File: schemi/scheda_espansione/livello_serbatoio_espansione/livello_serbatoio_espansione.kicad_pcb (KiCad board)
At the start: 2 copper layers, 70 x 50 mm, 264 parts, among them J1 exp1, J2 exp_spi, J3 exp2

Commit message: modifiche scheda definitiva (rev. C)
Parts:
- removed the REF** at (123.0, 62.9)
- removed the REF** at (156.0, 91.0)
- removed the REF** at (112.9, 78.2)
- removed the REF** at (171.3, 58.8)
- removed the REF** at (168.8, 58.8)
- removed the REF** at (166.2, 58.8)
- removed the REF** at (163.7, 58.8)
- removed the REF** at (161.2, 58.8)
- removed the REF** at (173.9, 58.8)
- removed the REF** at (173.8, 80.9)
- removed the REF** at (171.3, 80.9)
- removed the REF** at (168.8, 80.9)
- removed the REF** at (163.7, 91.0)
- removed the REF** at (166.2, 80.9)
- removed the REF** at (163.7, 80.9)
- removed the REF** at (161.1, 78.3)
- removed the REF** at (158.6, 78.3)
- removed the REF** at (156.1, 78.3)
- removed the REF** at (153.5, 78.3)
- removed the REF** at (118.0, 75.7)
- removed the REF** at (115.5, 75.7)
- removed the REF** at (112.9, 75.7)
- removed the REF** at (171.3, 56.3)
- removed the REF** at (171.3, 91.0)
- removed the REF** at (168.8, 56.3)
- removed the REF** at (166.2, 56.3)
- removed the REF** at (163.7, 56.3)
- removed the REF** at (161.2, 56.3)
- removed the REF** at (173.9, 56.3)
- removed the REF** at (173.8, 78.3)
- removed the REF** at (171.3, 78.3)
- removed the REF** at (168.8, 78.3)
- removed the REF** at (166.2, 78.3)
- removed the REF** at (163.7, 78.3)
- removed the REF** at (166.2, 91.0)
- removed the REF** at (161.1, 75.8)
- removed the REF** at (158.6, 75.8)
- removed the REF** at (156.1, 75.8)
- removed the REF** at (153.5, 75.8)
- removed the REF** at (118.0, 73.2)
- removed the REF** at (115.5, 73.2)
- removed the REF** at (112.9, 73.2)
- removed the REF** at (171.3, 53.8)
- removed the REF** at (168.8, 53.8)
- removed the REF** at (166.2, 53.8)
- removed the REF** at (153.5, 91.0)
- removed the REF** at (163.7, 53.8)
- removed the REF** at (161.2, 53.8)
- removed the REF** at (173.9, 53.8)
- removed the REF** at (173.8, 75.8)
- removed the REF** at (171.3, 75.8)
- removed the REF** at (168.8, 75.8)
- removed the REF** at (166.2, 75.8)
- removed the REF** at (163.7, 75.8)
- removed the REF** at (161.1, 73.3)
- removed the REF** at (158.6, 73.3)
- removed the REF** at (158.6, 91.0)
- removed the REF** at (156.1, 73.3)
- removed the REF** at (153.5, 73.3)
- removed the REF** at (118.0, 70.6)
- removed the REF** at (115.5, 70.6)
- removed the REF** at (112.9, 70.6)
- removed the REF** at (171.3, 51.2)
- removed the REF** at (168.8, 51.2)
- removed the REF** at (166.2, 51.2)
- removed the REF** at (163.7, 51.2)
- removed the REF** at (161.2, 51.2)
- removed the REF** at (161.1, 91.0)
- removed the REF** at (173.9, 51.2)
- removed the REF** at (173.8, 73.3)
- removed the REF** at (171.3, 73.3)
- removed the REF** at (168.8, 73.3)
- removed the REF** at (166.2, 73.3)
- removed the REF** at (163.7, 73.3)
- removed the REF** at (173.9, 68.0)
- removed the REF** at (171.3, 68.0)
- removed the REF** at (168.8, 68.0)
- removed the REF** at (166.2, 68.0)
- removed the REF** at (168.8, 91.0)
- removed the REF** at (163.7, 68.0)
- removed the REF** at (161.2, 68.0)
- removed the REF** at (158.6, 68.0)
- removed the REF** at (156.1, 68.0)
- removed the REF** at (153.5, 68.0)
- removed the REF** at (151.0, 68.0)
- removed the REF** at (148.5, 68.0)
- removed the REF** at (145.9, 68.0)
- removed the REF** at (143.4, 68.0)
- removed the REF** at (140.8, 68.0)
- removed the REF** at (173.8, 91.0)
- removed the REF** at (138.3, 68.0)
- removed the REF** at (135.8, 68.0)
- removed the REF** at (133.2, 68.0)
- removed the REF** at (130.7, 68.0)
- removed the REF** at (128.1, 68.0)
- removed the REF** at (125.6, 68.0)
- removed the REF** at (118.0, 68.1)
- removed the REF** at (115.5, 68.1)
- removed the REF** at (112.9, 68.1)
- removed the REF** at (173.9, 65.4)
- removed the REF** at (161.1, 88.5)
- removed the REF** at (171.3, 65.4)
- removed the REF** at (168.8, 65.4)
- removed the REF** at (166.2, 65.4)
- removed the REF** at (163.7, 65.4)
- removed the REF** at (161.2, 65.4)
- removed the REF** at (158.6, 65.4)
- removed the REF** at (156.1, 65.4)
- removed the REF** at (153.5, 65.4)
- removed the REF** at (151.0, 65.4)
- removed the REF** at (148.5, 65.4)
- removed the REF** at (123.0, 65.4)
- removed the REF** at (158.6, 88.5)
- removed the REF** at (145.9, 65.4)
- removed the REF** at (143.4, 65.4)
- removed the REF** at (140.8, 65.4)
- removed the REF** at (138.3, 65.4)
- removed the REF** at (135.8, 65.4)
- removed the REF** at (133.2, 65.4)
- removed the REF** at (130.7, 65.4)
- removed the REF** at (128.1, 65.4)
- removed the REF** at (125.6, 65.4)
- removed the REF** at (118.0, 65.5)
- removed the REF** at (156.1, 88.5)
- removed the REF** at (115.5, 65.5)
- removed the REF** at (112.9, 65.5)
- removed the REF** at (173.9, 62.9)
- removed the REF** at (171.3, 62.9)
- removed the REF** at (168.8, 62.9)
- removed the REF** at (166.2, 62.9)
- removed the REF** at (163.7, 62.9)
- removed the REF** at (161.2, 62.9)
- removed the REF** at (158.6, 62.9)
- removed the REF** at (156.1, 62.9)
- removed the REF** at (153.5, 88.5)
- removed the REF** at (153.5, 62.9)
- removed the REF** at (151.0, 62.9)
- removed the REF** at (148.5, 62.9)
- removed the REF** at (145.9, 62.9)
- removed the REF** at (143.4, 62.9)
- removed the REF** at (140.8, 62.9)
- removed the REF** at (138.3, 62.9)
- removed the REF** at (135.8, 62.9)
- removed the REF** at (133.2, 62.9)
- removed the REF** at (130.7, 62.9)
- removed the REF** at (151.0, 91.0)
- removed the REF** at (128.1, 62.9)
- removed the REF** at (125.6, 62.9)
- removed the REF** at (118.0, 63.0)
- removed the REF** at (115.5, 63.0)
- removed the REF** at (112.9, 63.0)
- removed the REF** at (148.4, 91.0)
- removed the REF** at (145.9, 91.0)
- removed the REF** at (143.3, 91.0)
- removed the REF** at (140.8, 91.0)
- removed the REF** at (138.3, 91.0)
- removed the REF** at (135.7, 91.0)
- removed the REF** at (123.0, 68.0)
- removed the REF** at (133.2, 91.0)
- removed the REF** at (130.6, 91.0)
- removed the REF** at (128.1, 91.0)
- removed the REF** at (125.6, 91.0)
- removed the REF** at (123.0, 91.0)
- removed the REF** at (120.5, 91.0)
- removed the REF** at (117.9, 91.0)
- removed the REF** at (115.4, 91.0)
- removed the REF** at (112.9, 91.0)
- removed the REF** at (173.8, 88.5)
- removed the REF** at (115.4, 83.3)
- removed the REF** at (171.3, 88.5)
- removed the REF** at (168.8, 88.5)
- removed the REF** at (166.2, 88.5)
- removed the REF** at (163.7, 88.5)
- removed the REF** at (161.1, 86.0)
- removed the REF** at (158.6, 86.0)
- removed the REF** at (156.1, 86.0)
- removed the REF** at (153.5, 86.0)
- removed the REF** at (151.0, 88.5)
- removed the REF** at (148.4, 88.5)
- removed the REF** at (112.9, 80.8)
- removed the REF** at (145.9, 88.5)
- removed the REF** at (143.3, 88.5)
- removed the REF** at (140.8, 88.5)
- removed the REF** at (138.3, 88.5)
- removed the REF** at (135.7, 88.5)
- removed the REF** at (133.2, 88.5)
- removed the REF** at (130.6, 88.5)
- removed the REF** at (128.1, 88.5)
- removed the REF** at (125.6, 88.5)
- removed the REF** at (123.0, 88.5)
- removed the REF** at (118.0, 80.8)
- removed the REF** at (120.5, 88.5)
- removed the REF** at (117.9, 88.5)
- removed the REF** at (115.4, 88.5)
- removed the REF** at (112.9, 88.5)
- removed the REF** at (173.8, 86.0)
- removed the REF** at (171.3, 86.0)
- removed the REF** at (168.8, 86.0)
- removed the REF** at (166.2, 86.0)
- removed the REF** at (163.7, 86.0)
- removed the REF** at (161.1, 83.4)
- removed the REF** at (115.4, 80.8)
- removed the REF** at (158.6, 83.4)
- removed the REF** at (156.1, 83.4)
- removed the REF** at (153.5, 83.4)
- removed the REF** at (151.0, 85.9)
- removed the REF** at (148.4, 85.9)
- removed the REF** at (145.9, 85.9)
- removed the REF** at (143.3, 85.9)
- removed the REF** at (140.8, 85.9)
- removed the REF** at (138.3, 85.9)
- removed the REF** at (135.7, 85.9)
- removed the REF** at (112.9, 83.3)
- removed the REF** at (133.2, 85.9)
- removed the REF** at (130.6, 85.9)
- removed the REF** at (128.1, 85.9)
- removed the REF** at (125.6, 85.9)
- removed the REF** at (123.0, 85.9)
- removed the REF** at (120.5, 85.9)
- removed the REF** at (117.9, 85.9)
- removed the REF** at (115.4, 85.9)
- removed the REF** at (112.9, 85.9)
- removed the REF** at (173.8, 83.4)
- removed the REF** at (118.0, 83.3)
- removed the REF** at (171.3, 83.4)
- removed the REF** at (168.8, 83.4)
- removed the REF** at (166.2, 83.4)
- removed the REF** at (163.7, 83.4)
- removed the REF** at (161.1, 80.9)
- removed the REF** at (158.6, 80.9)
- removed the REF** at (156.1, 80.9)
- removed the REF** at (153.5, 80.9)
- removed the REF** at (118.0, 78.2)
- removed the REF** at (115.5, 78.2)
- removed TP1, TP12, TP23, TP27, TP5: GND, TestPoint:TestPoint_THTPad_D1.5mm_Drill0.7mm
- removed TP10: SPI_SCK, TestPoint:TestPoint_THTPad_D1.5mm_Drill0.7mm
- removed TP11: SPI_MISO, TestPoint:TestPoint_THTPad_D1.5mm_Drill0.7mm
- removed TP13: D9, TestPoint:TestPoint_THTPad_D1.5mm_Drill0.7mm
- removed TP14: D8, TestPoint:TestPoint_THTPad_D1.5mm_Drill0.7mm
- removed TP15: D7, TestPoint:TestPoint_THTPad_D1.5mm_Drill0.7mm
- removed TP16: D6, TestPoint:TestPoint_THTPad_D1.5mm_Drill0.7mm
- removed TP17: D5, TestPoint:TestPoint_THTPad_D1.5mm_Drill0.7mm
- removed TP18: A0, TestPoint:TestPoint_THTPad_D1.5mm_Drill0.7mm
- removed TP19: A1, TestPoint:TestPoint_THTPad_D1.5mm_Drill0.7mm
- removed TP2: SPI_MOSI, TestPoint:TestPoint_THTPad_D1.5mm_Drill0.7mm
- removed TP20: A2, TestPoint:TestPoint_THTPad_D1.5mm_Drill0.7mm
- removed TP21: A3, TestPoint:TestPoint_THTPad_D1.5mm_Drill0.7mm
- removed TP22: D4, TestPoint:TestPoint_THTPad_D1.5mm_Drill0.7mm
- removed TP24: D3, TestPoint:TestPoint_THTPad_D1.5mm_Drill0.7mm
- removed TP25: RV, TestPoint:TestPoint_THTPad_D1.5mm_Drill0.7mm
- removed TP26, TP3: VDD, TestPoint:TestPoint_THTPad_D1.5mm_Drill0.7mm
- removed TP4: +5V, TestPoint:TestPoint_THTPad_D1.5mm_Drill0.7mm
- removed TP6: D10, TestPoint:TestPoint_THTPad_D1.5mm_Drill0.7mm
- removed TP7: A4, TestPoint:TestPoint_THTPad_D1.5mm_Drill0.7mm
- removed TP8: A5, TestPoint:TestPoint_THTPad_D1.5mm_Drill0.7mm
- removed TP9: RST, TestPoint:TestPoint_THTPad_D1.5mm_Drill0.7mm
- added J6: Exp_Analog_2, Connector_PinSocket_2.54mm:PinSocket_1x04_P2.54mm_Vertical, F.Cu at (91.1, 62.4)
- added JP1: A0_J, Jumper:SolderJumper-2_P1.3mm_Open_Pad1.0x1.5mm, F.Cu at (98.8, 59.0)
- added JP2: A1_J, Jumper:SolderJumper-2_P1.3mm_Open_Pad1.0x1.5mm, F.Cu at (96.2, 59.0)
- added JP3: A2_J, Jumper:SolderJumper-2_P1.3mm_Open_Pad1.0x1.5mm, F.Cu at (93.7, 59.0)
- added JP4: A3_J, Jumper:SolderJumper-2_P1.3mm_Open_Pad1.0x1.5mm, F.Cu at (91.1, 59.0)
- added REF**: OSHW-Logo2_7.3x6mm_SilkScreen, Symbol:OSHW-Logo2_7.3x6mm_SilkScreen, F.Cu at (137.0, 49.0)
- added REF**: KiCad-Logo2_5mm_SilkScreen, Symbol:KiCad-Logo2_5mm_SilkScreen, F.Cu at (140.9, 54.7)
- added REF**: ESD-Logo_6.6x6mm_SilkScreen, Symbol:ESD-Logo_6.6x6mm_SilkScreen, F.Cu at (144.2, 48.6)
- moved J2 73.9 mm to (71.6, 84.1), turned to 0 degrees
- moved J1 67.1 mm to (70.3, 68.9), turned to 0 degrees
- moved J3 42.5 mm to (75.9, 55.5)
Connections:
- J3 pad 10: A0 -> Net-(J3-Pin_10)
- J3 pad 7: A3 -> Net-(J3-Pin_7)
- J3 pad 8: A2 -> Net-(J3-Pin_8)
- J3 pad 9: A1 -> Net-(J3-Pin_9)
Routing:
- net VDD: track 76.8 -> 34.6 mm
- net GND: track 17.0 -> 0.01 mm
- net D7: track 3.58 -> 0.00 mm
- net D4: track 3.55 -> 0.00 mm
- net D3: track 3.54 -> 0.00 mm
- net RV: track 3.54 -> 0.00 mm
- net D9: track 3.54 -> 0.00 mm
- net D8: track 3.54 -> 0.00 mm
- net D6: track 3.53 -> 0.00 mm
- net D5: track 3.52 -> 0.00 mm
- net A4: track 3.30 -> 0.04 mm
- net A5: track 3.30 -> 0.05 mm
- net D10: track 3.25 -> 0.02 mm
- net SCK: track 3.14 -> 0.00 mm
- net MISO: track 3.14 -> 0.00 mm
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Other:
- board size 70 x 50 mm -> 83 x 52 mm
- net class Default removed
- board text added: "5V"
- board text added: "JLCJLCJLCJLC"
- board text added: "Prototipo (espansione v1.0_Rev.C)"
- board text added: "RS"
- board text removed: "Prototipo (espansione v1.0_Rev.A)"
- board text removed: "R"
- board text removed: "SPI"

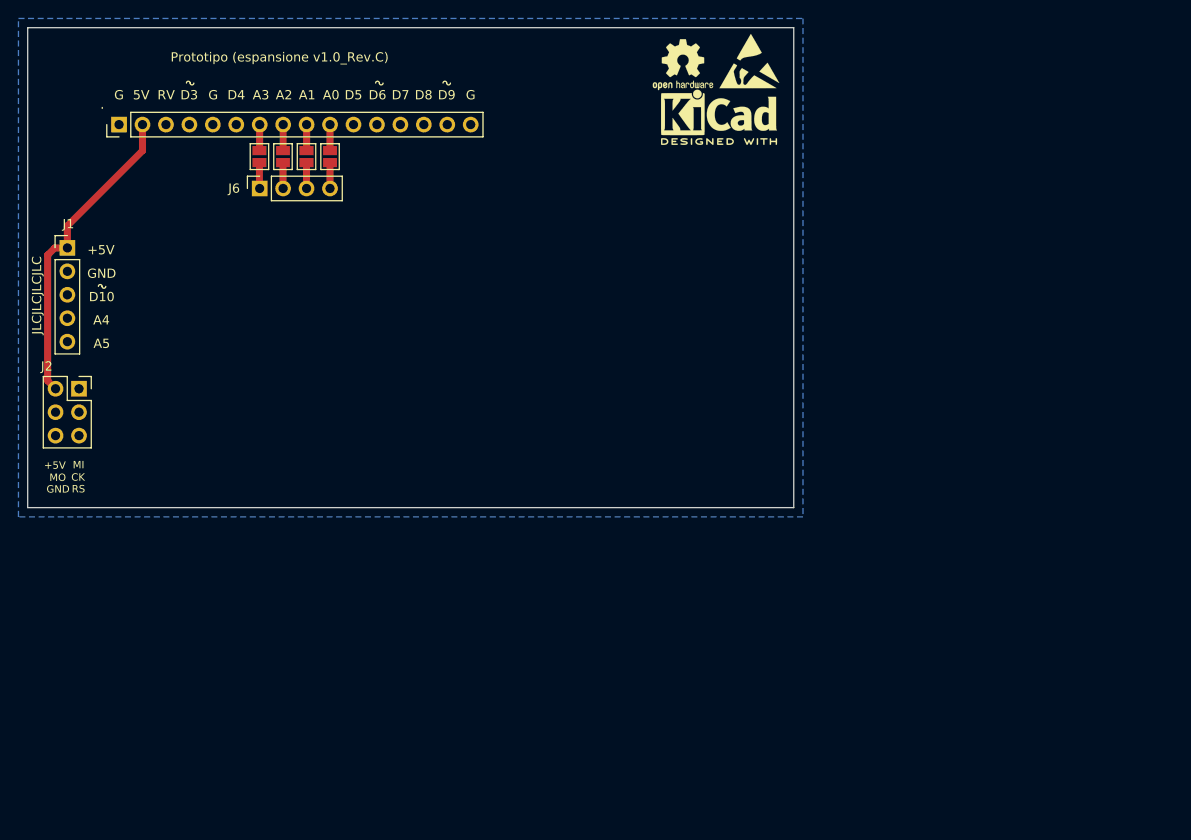
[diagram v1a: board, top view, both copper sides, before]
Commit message: scheda rev. D - applicate revisioni - allineati vincoli a capability jlc - adattata scheda prototipo
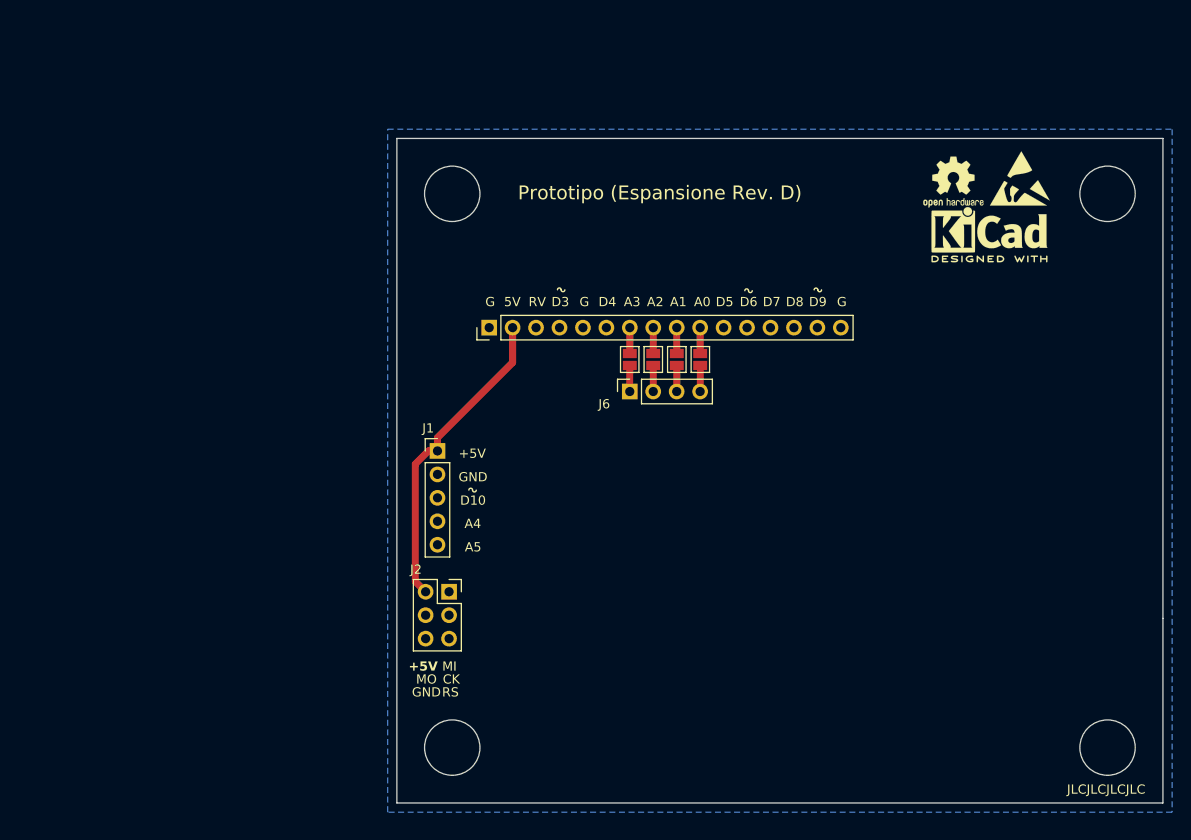
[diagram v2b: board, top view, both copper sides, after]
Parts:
- moved JP2 45.7 mm to (136.3, 81.0)
- moved JP3 45.7 mm to (133.8, 81.0)
- moved JP1 45.7 mm to (138.9, 81.0)
- moved JP4 45.7 mm to (131.2, 81.0)
- moved J1 45.7 mm to (110.4, 90.9)
- moved J6 45.7 mm to (131.2, 84.4)
- moved J3 45.7 mm to (116.0, 77.5)
- moved J2 45.7 mm to (111.7, 106.1)
- moved REF** 31.9 mm to (166.3, 61.7)
- moved REF** 31.9 mm to (173.5, 61.3)
- moved REF** 31.9 mm to (170.2, 67.4)
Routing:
- net VDD: track 34.6 -> 34.0 mm
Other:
- board size 83 x 52 mm -> 83 x 72 mm
- board text added: "Prototipo (Espansione Rev. D)"
- board text removed: "Prototipo (espansione v1.0_Rev.C)"

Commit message: revisioni pcb (rimosse violazione jlcpcb) aggiunti stl per case e coperchio da fusion360
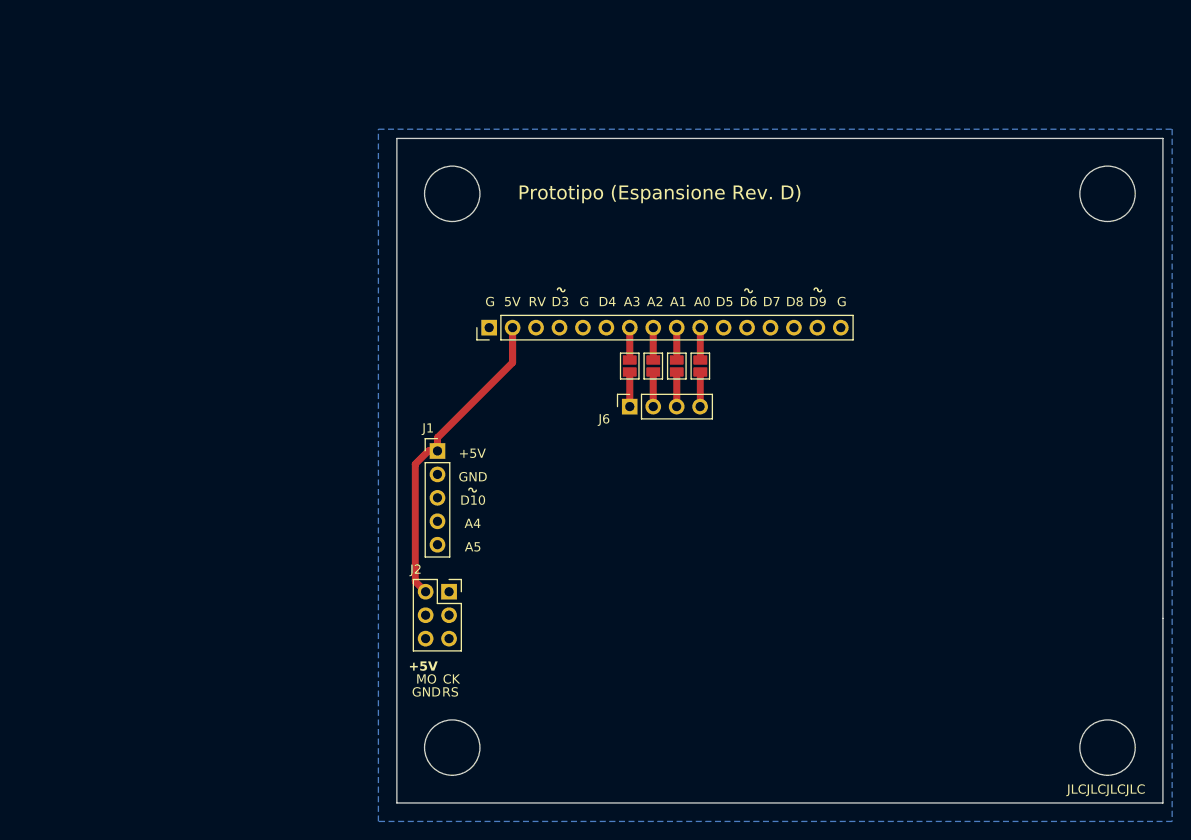
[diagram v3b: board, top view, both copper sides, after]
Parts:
- removed REF**: OSHW-Logo2_7.3x6mm_SilkScreen, Symbol:OSHW-Logo2_7.3x6mm_SilkScreen
- removed REF**: KiCad-Logo2_5mm_SilkScreen, Symbol:KiCad-Logo2_5mm_SilkScreen
- removed REF**: ESD-Logo_6.6x6mm_SilkScreen, Symbol:ESD-Logo_6.6x6mm_SilkScreen
- moved J6 1.64 mm to (131.2, 86.1)
- moved JP1 0.71 mm to (138.9, 81.7)
- moved JP2 0.71 mm to (136.3, 81.7)
- moved JP3 0.71 mm to (133.8, 81.7)
- moved JP4 0.71 mm to (131.2, 81.7)
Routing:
- net A1: track 2.83 -> 3.75 mm
- net A0: track 2.83 -> 3.76 mm
- net A3: track 2.82 -> 3.75 mm
- net A2: track 2.82 -> 3.75 mm
- net Net-(J3-Pin_8): track 2.80 -> 3.51 mm
- net Net-(J3-Pin_10): track 2.81 -> 3.52 mm
- net Net-(J3-Pin_9): track 2.80 -> 3.51 mm
- net Net-(J3-Pin_7): track 2.80 -> 3.51 mm
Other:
- board text removed: "MI"
